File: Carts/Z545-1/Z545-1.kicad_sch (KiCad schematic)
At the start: 25 parts, among them IC1 uPD23C16000WGX, IC2 HM62256BLFP-10T, IC3 74HC00A, J1 Loopy-Cart-Edge

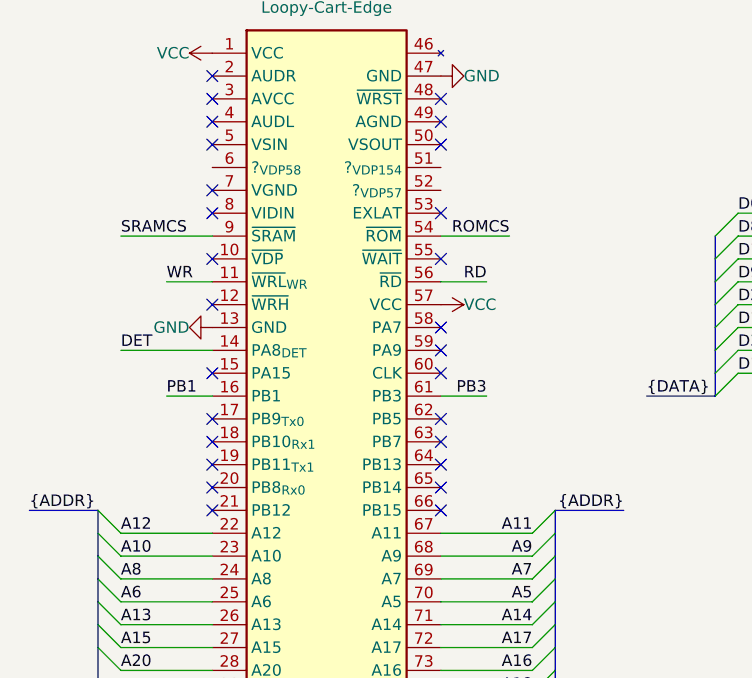
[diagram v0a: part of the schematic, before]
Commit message: Unify project part libs
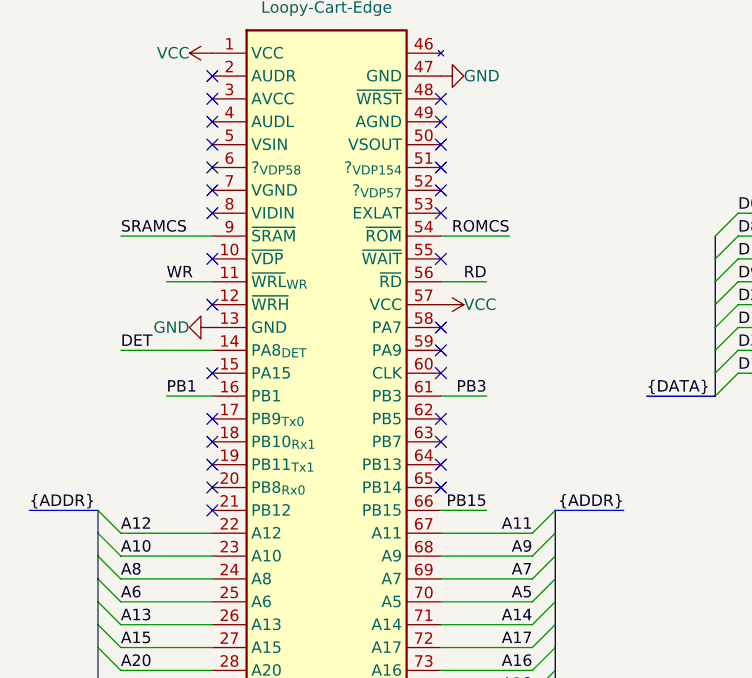
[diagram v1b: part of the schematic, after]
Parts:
- IC1: symbol project-parts:ROM_32Mbit_SOP44_Physical -> loopy-parts:ROM_32Mbit_SOP44_Physical
- IC2: symbol project-parts:SRAM_256Kbit_SOP28_Physical -> loopy-parts:SRAM_256Kbit_SOP28_Physical
- J1: footprint project-parts:Loopy-Cart-Edge -> loopy-parts:Loopy_Cart_Edge; symbol project-parts:Loopy-Cart-Edge -> loopy-parts:Loopy_Cart_Edge
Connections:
- net PB15: now also J1.66 (PB15)
- no-connect marks 34 -> 36
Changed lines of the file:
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@@
 	)
 	(no_connect
-		(at 60.96 91.44)
-	)
-	(no_connect
 		(at 60.96 124.46)
 	)
@@
 	)
 	(no_connect
+		(at 35.56 53.34)
+	)
+	(no_connect
 		(at 60.96 73.66)
 	)
 	(no_connect
+		(at 60.96 53.34)
+	)
+	(no_connect
 		(at 236.22 139.7)
 	)
@@
 	)
 	(no_connect
+		(at 60.96 55.88)
+	)
+	(no_connect
 		(at 60.96 58.42)
 	)
@@
 	(wire
 		(pts
+			(xy 60.96 91.44) (xy 66.04 91.44)
+		)
+		(stroke
+			(width 0)
+			(type default)
+		)
+	)
+	(wire
+		(pts
 			(xy 241.3 104.14) (xy 241.3 109.22)
 		)
@@
 		)
 	)
+	(label "PB15"
+		(at 66.04 91.44 180)
+		(effects
+			(font
+				(size 1.27 1.27)
+			)
+			(justify right bottom)
+		)
+	)
 	(label "{ADDR}"
 		(at 15.24 91.44 0)
@@
 	)
 	(symbol
-		(lib_id "project-parts:ROM_32Mbit_SOP44_Physical")
+		(lib_id "loopy-parts:ROM_32Mbit_SOP44_Physical")
 		(at 129.54 49.53 0)
 		(unit 1)
@@
 	)
 	(symbol
-		(lib_id "project-parts:SRAM_256Kbit_SOP28_Physical")
+		(lib_id "loopy-parts:SRAM_256Kbit_SOP28_Physical")
 		(at 208.28 39.37 0)
 		(unit 1)
@@
 	)
 	(symbol
-		(lib_id "project-parts:Loopy-Cart-Edge")
+		(lib_id "loopy-parts:Loopy_Cart_Edge")
 		(at 48.26 96.52 0)
 		(unit 1)
@@
 			)
 		)
-		(property "Footprint" "project-parts:Loopy-Cart-Edge"
+		(property "Footprint" "loopy-parts:Loopy_Cart_Edge"
 			(at 48.26 38.1 0)
 			(effects
